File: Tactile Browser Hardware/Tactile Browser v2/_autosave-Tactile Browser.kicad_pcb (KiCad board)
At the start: 4 copper layers, 82.5 x 114 mm, 130 parts, among them SW1 SW_Push, SW10 SW_Push, SW11 SW_Push, SW12 SW_Push, SW13 SW_Push, SW14 SW_Push, SW15 SW_Push, SW16 SW_Push, SW17 SW_Push, SW18 SW_Push, SW2 SW_Push, SW3 SW_Push, SW4 SW_Push, SW5 SW_Push, SW6 SW_Push, SW7 SW_Push, SW8 SW_Push, SW9 SW_Push

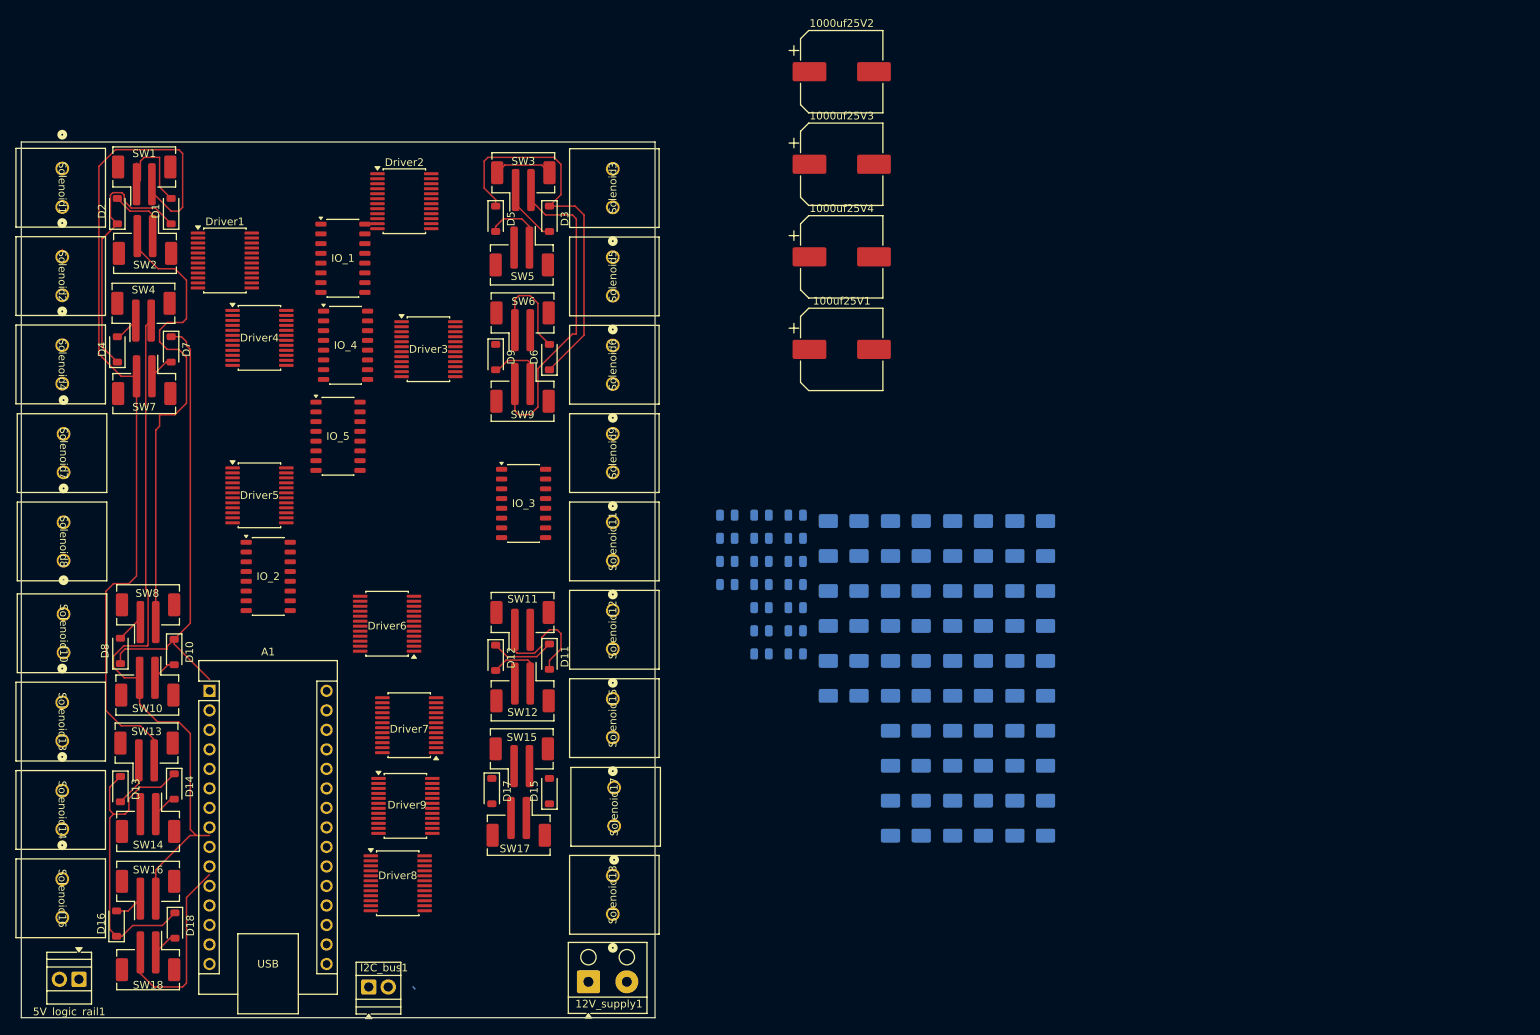
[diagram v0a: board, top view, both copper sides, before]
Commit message: changed to vertical screw terminals
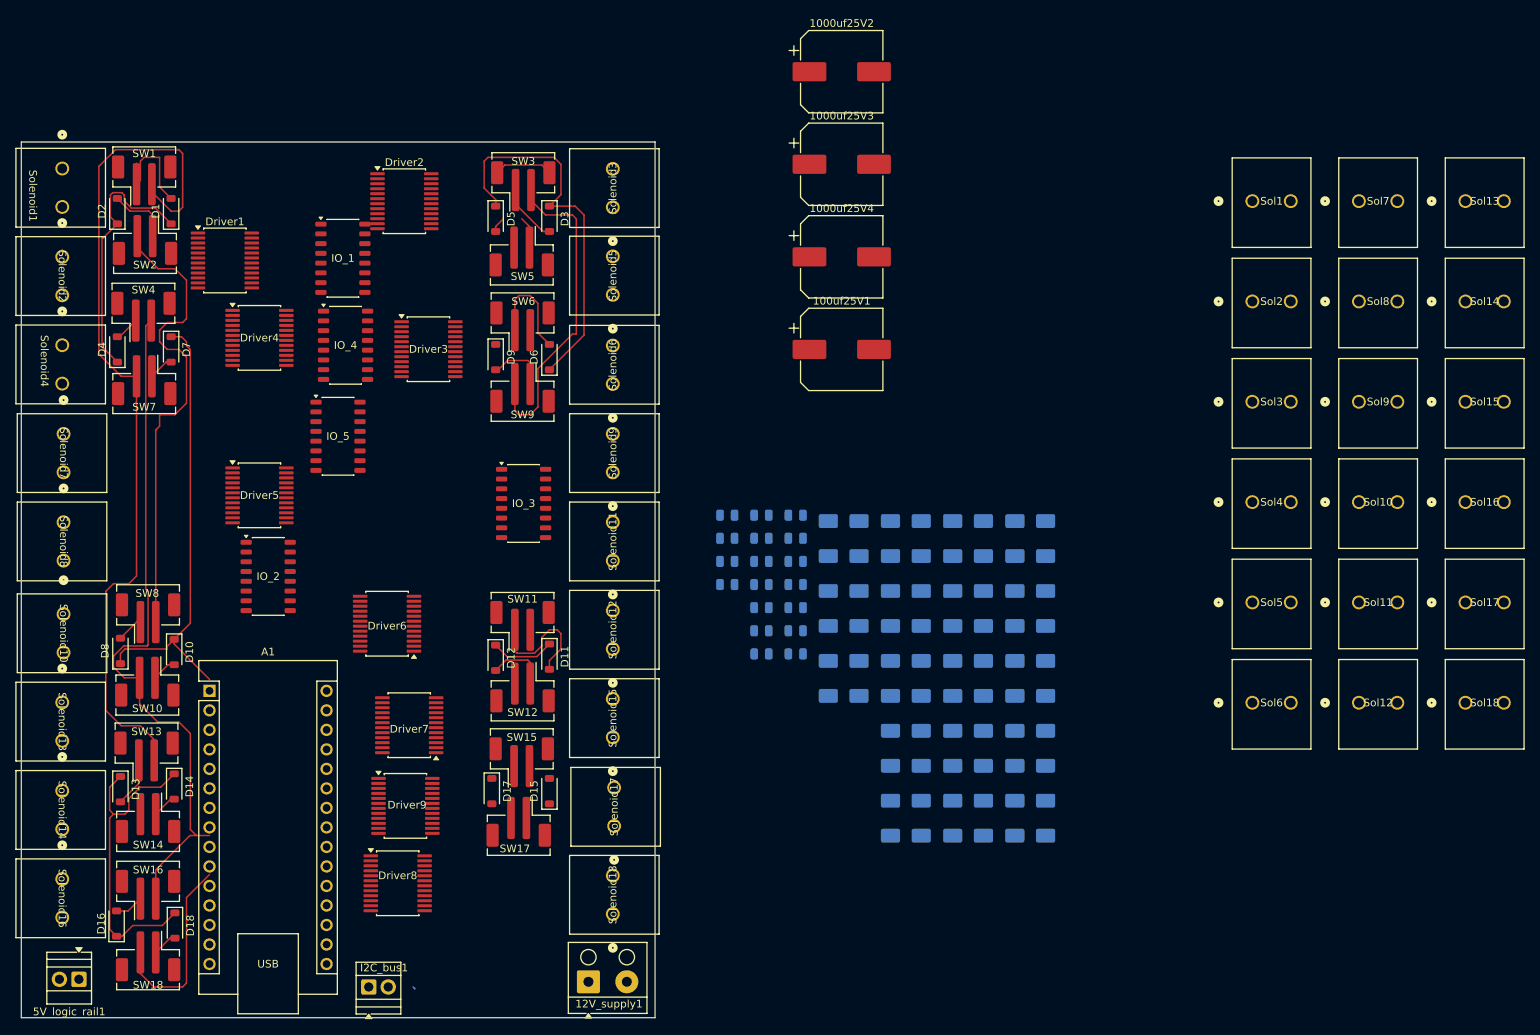
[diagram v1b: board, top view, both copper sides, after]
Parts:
- added Sol1: Conn_01x02_Pin, TerminalBlock_Phoenix:ScrewTerminal_Vertical_1935310, F.Cu at (197.3, 41.7)
- added Sol10: Conn_01x02_Pin, TerminalBlock_Phoenix:ScrewTerminal_Vertical_1935310, F.Cu at (211.1, 80.9)
- added Sol11: Conn_01x02_Pin, TerminalBlock_Phoenix:ScrewTerminal_Vertical_1935310, F.Cu at (211.1, 93.9)
- added Sol12: Conn_01x02_Pin, TerminalBlock_Phoenix:ScrewTerminal_Vertical_1935310, F.Cu at (211.1, 107.0)
- added Sol13: Conn_01x02_Pin, TerminalBlock_Phoenix:ScrewTerminal_Vertical_1935310, F.Cu at (225.0, 41.7)
- added Sol14: Conn_01x02_Pin, TerminalBlock_Phoenix:ScrewTerminal_Vertical_1935310, F.Cu at (225.0, 54.8)
- added Sol15: Conn_01x02_Pin, TerminalBlock_Phoenix:ScrewTerminal_Vertical_1935310, F.Cu at (225.0, 67.8)
- added Sol16: Conn_01x02_Pin, TerminalBlock_Phoenix:ScrewTerminal_Vertical_1935310, F.Cu at (225.0, 80.9)
- added Sol17: Conn_01x02_Pin, TerminalBlock_Phoenix:ScrewTerminal_Vertical_1935310, F.Cu at (225.0, 93.9)
- added Sol18: Conn_01x02_Pin, TerminalBlock_Phoenix:ScrewTerminal_Vertical_1935310, F.Cu at (225.0, 107.0)
- added Sol2: Conn_01x02_Pin, TerminalBlock_Phoenix:ScrewTerminal_Vertical_1935310, F.Cu at (197.3, 54.8)
- added Sol3: Conn_01x02_Pin, TerminalBlock_Phoenix:ScrewTerminal_Vertical_1935310, F.Cu at (197.3, 67.8)
- added Sol4: Conn_01x02_Pin, TerminalBlock_Phoenix:ScrewTerminal_Vertical_1935310, F.Cu at (197.3, 80.9)
- added Sol5: Conn_01x02_Pin, TerminalBlock_Phoenix:ScrewTerminal_Vertical_1935310, F.Cu at (197.3, 93.9)
- added Sol6: Conn_01x02_Pin, TerminalBlock_Phoenix:ScrewTerminal_Vertical_1935310, F.Cu at (197.3, 107.0)
- added Sol7: Conn_01x02_Pin, TerminalBlock_Phoenix:ScrewTerminal_Vertical_1935310, F.Cu at (211.1, 41.7)
- added Sol8: Conn_01x02_Pin, TerminalBlock_Phoenix:ScrewTerminal_Vertical_1935310, F.Cu at (211.1, 54.8)
- added Sol9: Conn_01x02_Pin, TerminalBlock_Phoenix:ScrewTerminal_Vertical_1935310, F.Cu at (211.1, 67.8)
- moved Solenoid5 0.10 mm to (114.0, 53.9)
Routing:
- net Net-(D5-A): track 8.63 -> 6.23 mm
